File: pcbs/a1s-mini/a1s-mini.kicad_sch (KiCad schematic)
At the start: 47 parts, among them J1 UART1, J2 SJ-3524-SMT-TR-PI, J3 Audio Out, J4 UART0, Q3 BC818, Q4 MBT3904DW1, Q6 MBT3904DW1, U1 ESP32 A1S, U2 AZ1117CH-3.3TRG1

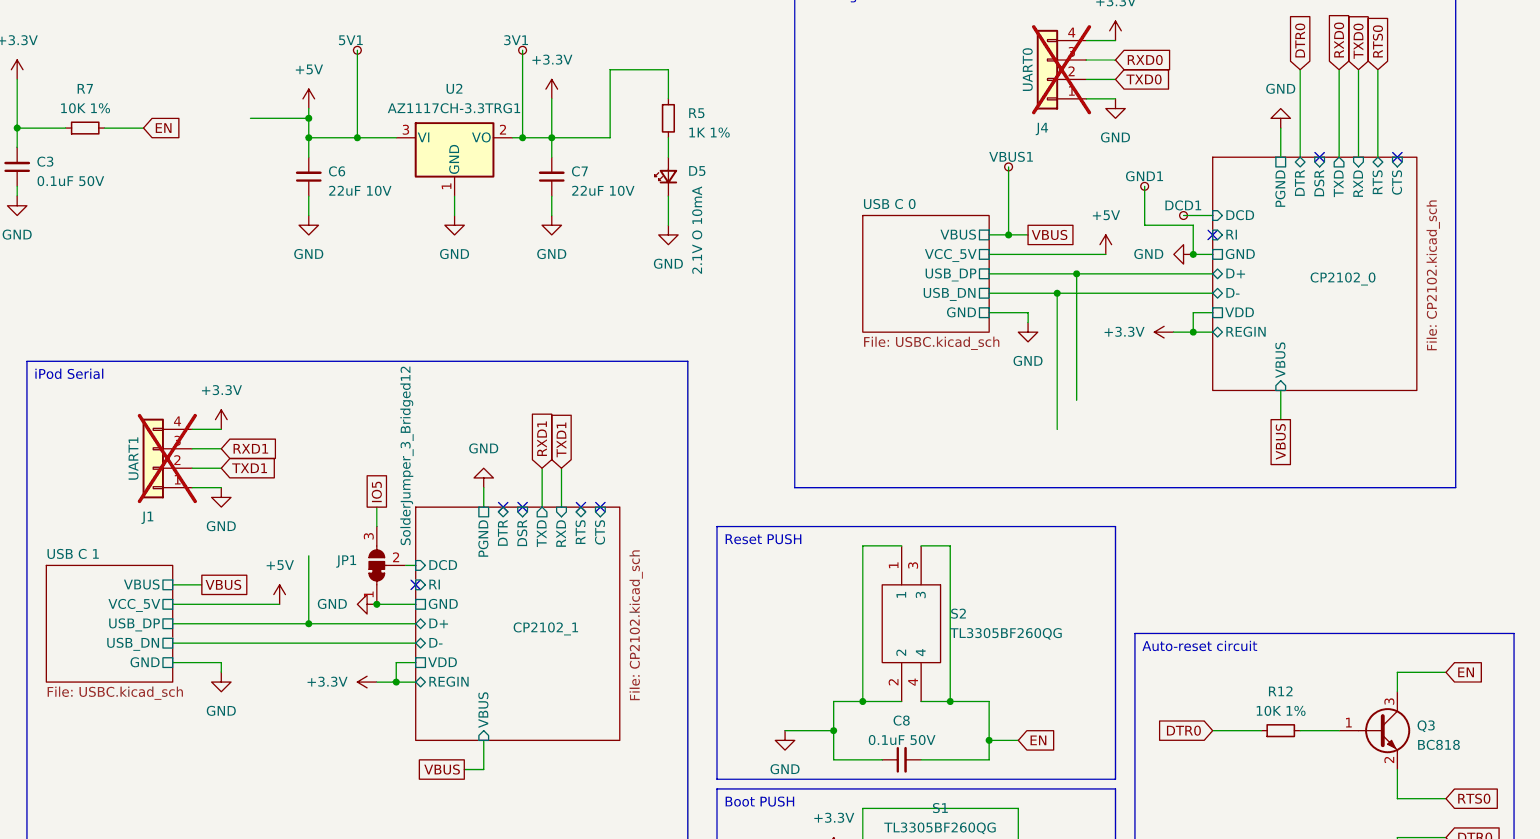
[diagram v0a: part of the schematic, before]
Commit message: Move to CP2102 non N
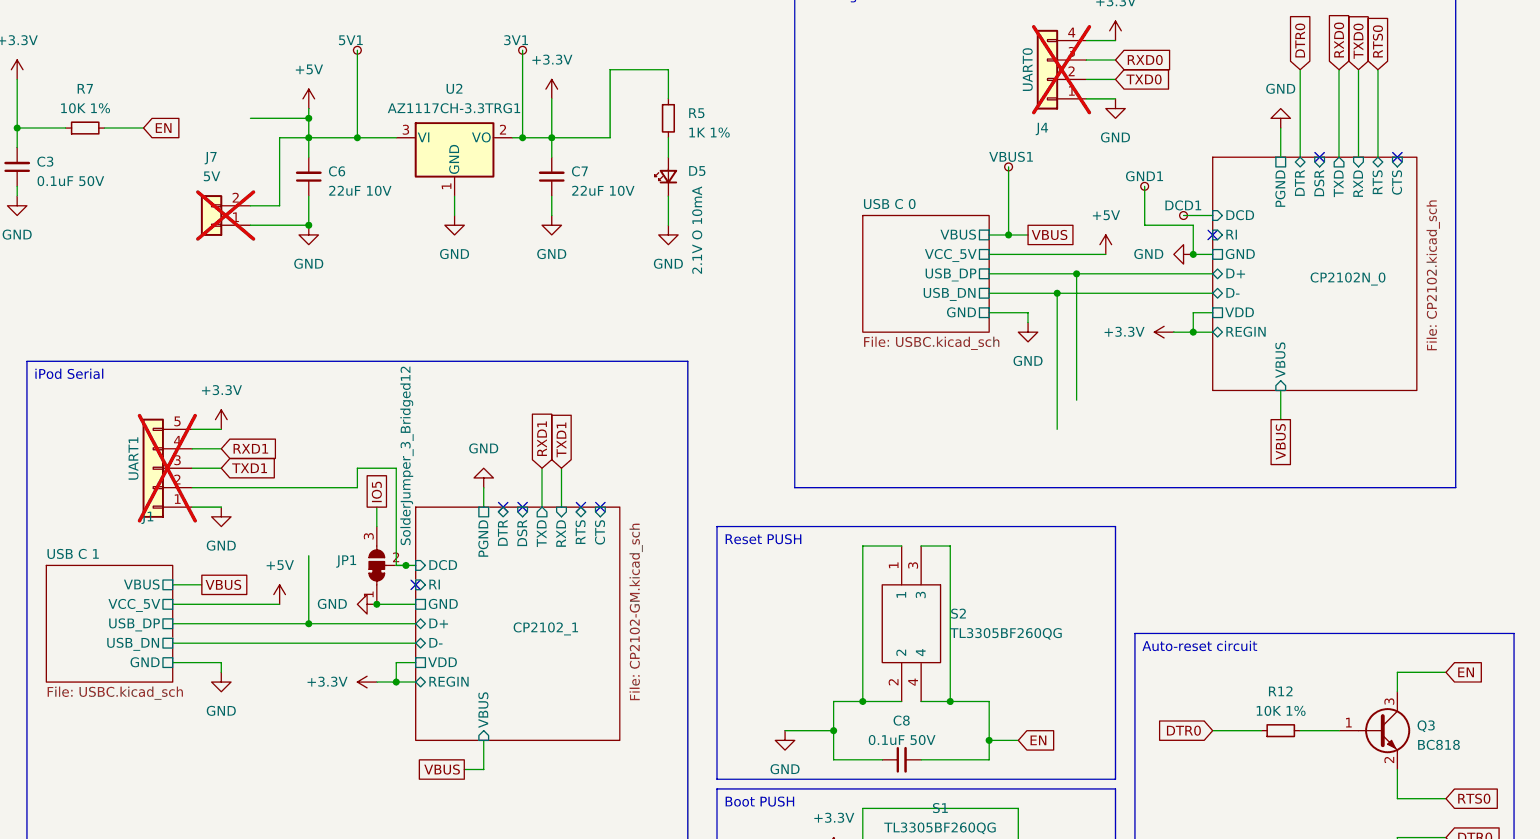
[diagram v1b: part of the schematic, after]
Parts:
- added J7: 5V, Connector_PinHeader_2.54mm:PinHeader_1x02_P2.54mm_Vertical, symbol Connector_Generic:Conn_01x02
- J1: symbol Connector_Generic:Conn_01x04 -> Connector_Generic:Conn_01x05
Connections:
- net +3.3V: now also J1.5 (Pin_5); no longer J1.4 (Pin_4)
- net +5V: now also J7.2 (Pin_2)
- net CP2102_1/DCD: now also J1.2 (Pin_2)
- net GND: now also J7.1 (Pin_1)
- net RXD1: now also J1.4 (Pin_4); no longer J1.3 (Pin_3)
- net TXD1: now also J1.3 (Pin_3); no longer J1.2 (Pin_2)
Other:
- sheet CP2102_0 renamed CP2102N_0
- sheet CP2102_1: file CP2102.kicad_sch -> CP2102-GM.kicad_sch
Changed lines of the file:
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@@
 	)
 	(junction
+		(at 138.43 90.17)
+		(diameter 0)
+		(color 0 0 0 0)
+	)
+	(junction
+		(at 125.73 45.72)
+		(diameter 0)
+		(color 0 0 0 0)
+	)
+	(junction
 		(at 241.3 59.69)
 		(diameter 0)
@@
 	(wire
 		(pts
-			(xy 125.73 41.91) (xy 125.73 44.45)
-		)
-		(stroke
-			(width 0)
-			(type default)
-		)
-	)
-	(wire
-		(pts
 			(xy 157.48 34.29) (xy 157.48 36.83)
 		)
@@
 	(wire
 		(pts
+			(xy 121.92 43.18) (xy 121.92 34.29)
+		)
+		(stroke
+			(width 0)
+			(type default)
+		)
+	)
+	(wire
+		(pts
 			(xy 200.66 152.4) (xy 200.66 153.67)
 		)
@@
 	(wire
 		(pts
+			(xy 125.73 41.91) (xy 125.73 45.72)
+		)
+		(stroke
+			(width 0)
+			(type default)
+		)
+	)
+	(wire
+		(pts
 			(xy 134.62 105.41) (xy 137.16 105.41)
 		)
@@
 	(wire
 		(pts
+			(xy 132.08 77.47) (xy 137.16 77.47)
+		)
+		(stroke
+			(width 0)
+			(type default)
+		)
+	)
+	(wire
+		(pts
 			(xy 78.74 147.32) (xy 78.74 149.86)
 		)
@@
 	(wire
 		(pts
+			(xy 118.11 45.72) (xy 125.73 45.72)
+		)
+		(stroke
+			(width 0)
+			(type default)
+		)
+	)
+	(wire
+		(pts
 			(xy 27.94 22.86) (xy 29.21 22.86)
 		)
@@
 	(wire
 		(pts
+			(xy 118.11 43.18) (xy 121.92 43.18)
+		)
+		(stroke
+			(width 0)
+			(type default)
+		)
+	)
+	(wire
+		(pts
 			(xy 67.31 38.1) (xy 71.12 38.1)
 		)
@@
 	(wire
 		(pts
+			(xy 137.16 77.47) (xy 137.16 90.17)
+		)
+		(stroke
+			(width 0)
+			(type default)
+		)
+	)
+	(wire
+		(pts
 			(xy 203.2 87.63) (xy 198.12 87.63)
 		)
@@
 	(wire
 		(pts
+			(xy 137.16 90.17) (xy 138.43 90.17)
+		)
+		(stroke
+			(width 0)
+			(type default)
+		)
+	)
+	(wire
+		(pts
 			(xy 262.89 25.4) (xy 262.89 36.83)
 		)
@@
 	(wire
 		(pts
+			(xy 110.49 80.01) (xy 132.08 80.01)
+		)
+		(stroke
+			(width 0)
+			(type default)
+		)
+	)
+	(wire
+		(pts
 			(xy 255.27 111.76) (xy 260.35 111.76)
 		)
@@
 	(wire
 		(pts
-			(xy 110.49 80.01) (xy 114.3 80.01)
+			(xy 149.86 173.99) (xy 151.13 173.99)
 		)
 		(stroke
@@
 	(wire
 		(pts
-			(xy 149.86 173.99) (xy 151.13 173.99)
+			(xy 219.71 57.15) (xy 219.71 58.42)
 		)
 		(stroke
@@
 	(wire
 		(pts
-			(xy 219.71 57.15) (xy 219.71 58.42)
+			(xy 29.21 25.4) (xy 17.78 25.4)
 		)
 		(stroke
@@
 	(wire
 		(pts
-			(xy 29.21 25.4) (xy 17.78 25.4)
+			(xy 267.97 158.75) (xy 267.97 161.29)
 		)
 		(stroke
@@
 	(wire
 		(pts
-			(xy 267.97 158.75) (xy 267.97 161.29)
+			(xy 234.95 45.72) (xy 234.95 40.64)
 		)
 		(stroke
@@
 	(wire
 		(pts
-			(xy 234.95 45.72) (xy 234.95 40.64)
+			(xy 125.73 88.9) (xy 125.73 97.79)
 		)
 		(stroke
@@
 	(wire
 		(pts
-			(xy 125.73 88.9) (xy 125.73 97.79)
+			(xy 121.92 34.29) (xy 125.73 34.29)
 		)
 		(stroke
@@
 	(wire
 		(pts
+			(xy 110.49 82.55) (xy 114.3 82.55)
+		)
+		(stroke
+			(width 0)
+			(type default)
+		)
+	)
+	(wire
+		(pts
 			(xy 267.97 104.14) (xy 267.97 106.68)
 		)
@@
 	(wire
 		(pts
+			(xy 132.08 80.01) (xy 132.08 77.47)
+		)
+		(stroke
+			(width 0)
+			(type default)
+		)
+	)
+	(wire
+		(pts
 			(xy 252.73 33.02) (xy 252.73 36.83)
 		)
@@
 	)
 	(symbol
+		(lib_id "Connector_Generic:Conn_01x02")
+		(at 113.03 45.72 180)
+		(unit 1)
+		(exclude_from_sim no)
+		(in_bom no)
+		(on_board yes)
+		(dnp yes)
+		(fields_autoplaced yes)
+		(property "Reference" "J7"
+			(at 113.03 36.83 0)
+			(effects
+				(font
+					(size 1.27 1.27)
+				)
+			)
+		)
+		(property "Value" "5V"
+			(at 113.03 39.37 0)
+			(effects
+				(font
+					(size 1.27 1.27)
+				)
+			)
+		)
+		(property "Footprint" "Connector_PinHeader_2.54mm:PinHeader_1x02_P2.54mm_Vertical"
+			(at 113.03 45.72 0)
+			(effects
+				(font
+					(size 1.27 1.27)
+				)
+				(hide yes)
+			)
+		)
+		(property "Datasheet" "~"
+			(at 113.03 45.72 0)
+			(effects
+				(font
+					(size 1.27 1.27)
+				)
+				(hide yes)
+			)
+		)
+		(property "Description" "Generic connector, single row, 01x02, script generated (kicad-library-utils/schlib/autogen/connector/)"
+			(at 113.03 45.72 0)
+			(effects
+				(font
+					(size 1.27 1.27)
+				)
+				(hide yes)
+			)
+		)
+		(pin "1"
+		)
+		(pin "2"
+		)
+		(instances
+			(project ""
+				(path "/473bba75-08f8-4c6c-a9b2-aa3e95e63a5e"
+					(reference "J7")
+					(unit 1)
+				)
+			)
+		)
+	)
+	(symbol
 		(lib_id "power:GND")
-		(at 114.3 80.01 0)
+		(at 114.3 82.55 0)
 		(unit 1)
 		(exclude_from_sim no)
@@
 		(fields_autoplaced yes)
 		(property "Reference" "#PWR027"
-			(at 114.3 86.36 0)
+			(at 114.3 88.9 0)
 			(effects
 				(font
@@
 		)
 		(property "Value" "GND"
-			(at 114.3 85.09 0)
+			(at 114.3 87.63 0)
 			(effects
 				(font
@@
 		)
 		(property "Footprint" ""
-			(at 114.3 80.01 0)
+			(at 114.3 82.55 0)
 			(effects
 				(font
@@
 		)
 		(property "Datasheet" ""
-			(at 114.3 80.01 0)
+			(at 114.3 82.55 0)
 			(effects
 				(font
@@
 		)
 		(property "Description" ""
-			(at 114.3 80.01 0)
+			(at 114.3 82.55 0)
 			(effects
 				(font
@@
 	(symbol
 		(lib_id "power:GND")
-		(at 125.73 44.45 0)
+		(at 125.73 45.72 0)
 		(unit 1)
 		(exclude_from_sim no)
@@
 		(fields_autoplaced yes)
 		(property "Reference" "#PWR031"
-			(at 125.73 50.8 0)
+			(at 125.73 52.07 0)
 			(effects
 				(font
@@
 		)
 		(property "Value" "GND"
-			(at 125.73 49.53 0)
+			(at 125.73 50.8 0)
 			(effects
 				(font
@@
 		)
 		(property "Footprint" ""
-			(at 125.73 44.45 0)
+			(at 125.73 45.72 0)
 			(effects
 				(font
@@
 		)
 		(property "Datasheet" ""
-			(at 125.73 44.45 0)
+			(at 125.73 45.72 0)
 			(effects
 				(font
@@
 		)
 		(property "Description" ""
-			(at 125.73 44.45 0)
+			(at 125.73 45.72 0)
 			(effects
 				(font
@@
 	)
 	(symbol
-		(lib_id "Connector_Generic:Conn_01x04")
+		(lib_id "Connector_Generic:Conn_01x05")
 		(at 105.41 77.47 180)
 		(unit 1)
@@
 			)
 		)
-		(property "Description" ""
+		(property "Description" "Generic connector, single row, 01x05, script generated (kicad-library-utils/schlib/autogen/connector/)"
 			(at 105.41 77.47 0)
 			(effects
@@
 					(size 1.27 1.27)
 				)
+				(hide yes)
 			)
 		)
@@
 		(pin "4"
 		)
+		(pin "5"
+		)
 		(instances
 			(project "a1s-mini"
@@
 			)
 		)
-		(property "Sheetfile" "CP2102.kicad_sch"
+		(property "Sheetfile" "CP2102-GM.kicad_sch"
 			(at 167.64 107.95 90)
 			(effects
@@
 			(color 0 0 0 0.0000)
 		)
-		(property "Sheetname" "CP2102_0"
+		(property "Sheetname" "CP2102N_0"
 			(at 256.54 53.34 0)
 			(effects

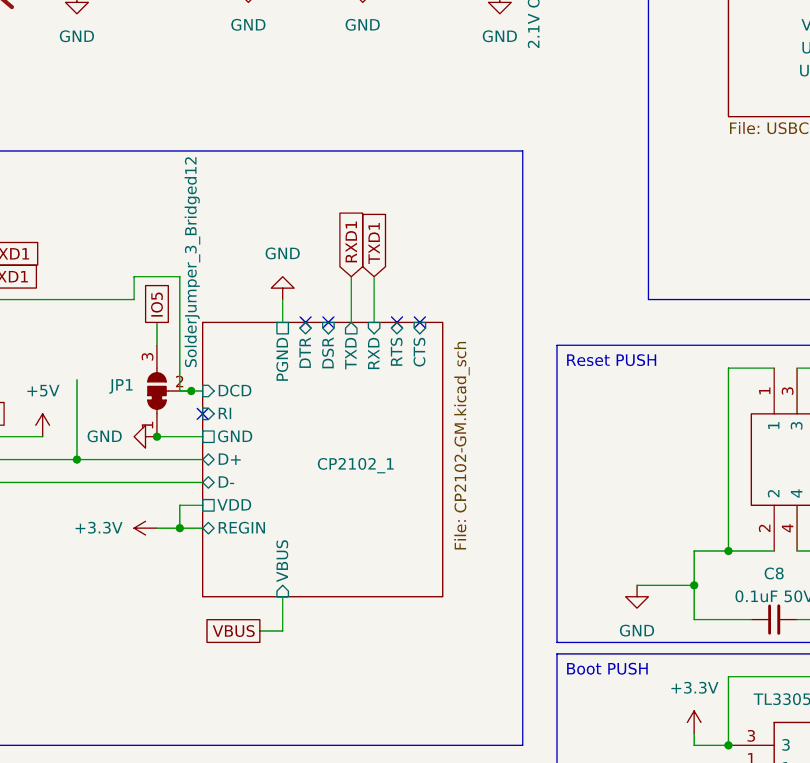
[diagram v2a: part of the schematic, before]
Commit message: A1S updated to CP2104
Version numbers also updated
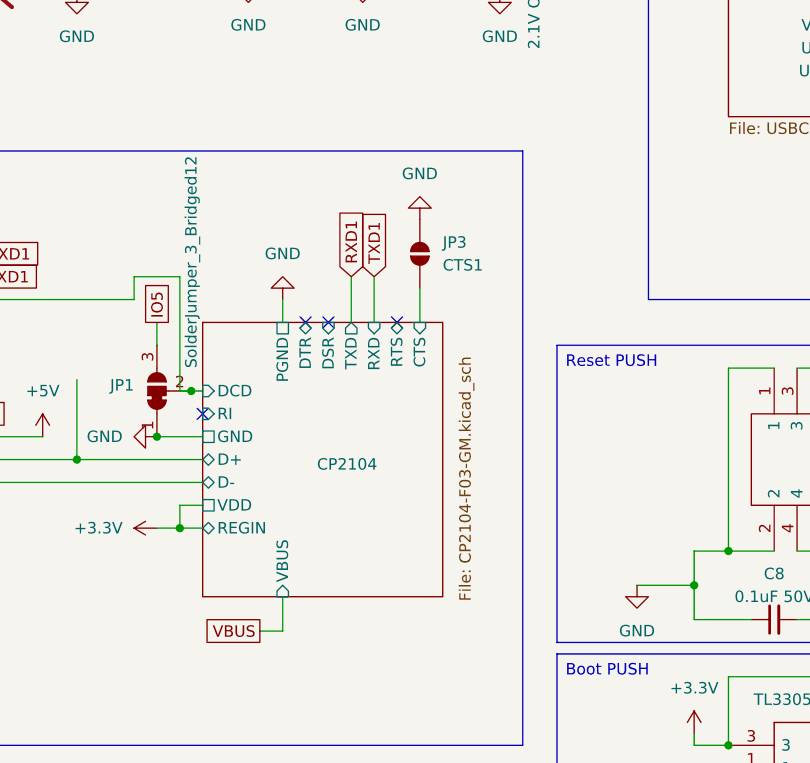
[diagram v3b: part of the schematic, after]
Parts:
- added JP3: CTS1, Jumper:SolderJumper-2_P1.3mm_Open_RoundedPad1.0x1.5mm, symbol Jumper:SolderJumper_2_Open
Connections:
- net CP2104/CTS: now also JP3.1 (A)
- net GND: now also JP3.2 (B)
- no-connect marks 30 -> 29
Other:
- sheet CP2102_1 renamed CP2104
- sheet CP2104: file CP2102-GM.kicad_sch -> CP2104-F03-GM.kicad_sch
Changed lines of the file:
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@@
 	(title_block
 		(title "A1S Mini Board")
-		(date "2025-10-05")
-		(rev "0.3.2")
+		(date "2025-10-22")
+		(rev "0.4.0")
 		(company "Martin Roger")
 	)
@@
 	)
 	(no_connect
-		(at 163.83 82.55)
-	)
-	(no_connect
 		(at 67.31 60.96)
 	)
@@
 	(wire
 		(pts
+			(xy 163.83 78.74) (xy 163.83 82.55)
+		)
+		(stroke
+			(width 0)
+			(type default)
+		)
+	)
+	(wire
+		(pts
 			(xy 110.49 151.13) (xy 110.49 152.4)
 		)
@@
 	(symbol
 		(lib_id "power:GND")
+		(at 163.83 71.12 180)
+		(unit 1)
+		(exclude_from_sim no)
+		(in_bom yes)
+		(on_board yes)
+		(dnp no)
+		(fields_autoplaced yes)
+		(property "Reference" "#PWR053"
+			(at 163.83 64.77 0)
+			(effects
+				(font
+					(size 1.27 1.27)
+				)
+				(hide yes)
+			)
+		)
+		(property "Value" "GND"
+			(at 163.83 66.04 0)
+			(effects
+				(font
+					(size 1.27 1.27)
+				)
+			)
+		)
+		(property "Footprint" ""
+			(at 163.83 71.12 0)
+			(effects
+				(font
+					(size 1.27 1.27)
+				)
+				(hide yes)
+			)
+		)
+		(property "Datasheet" ""
+			(at 163.83 71.12 0)
+			(effects
+				(font
+					(size 1.27 1.27)
+				)
+				(hide yes)
+			)
+		)
+		(property "Description" ""
+			(at 163.83 71.12 0)
+			(effects
+				(font
+					(size 1.27 1.27)
+				)
+			)
+		)
+		(pin "1"
+		)
+		(instances
+			(project "a1s-mini"
+				(path "/473bba75-08f8-4c6c-a9b2-aa3e95e63a5e"
+					(reference "#PWR053")
+					(unit 1)
+				)
+			)
+		)
+	)
+	(symbol
+		(lib_id "power:GND")
 		(at 252.73 33.02 180)
 		(unit 1)
@@
 	)
 	(symbol
+		(lib_id "Jumper:SolderJumper_2_Open")
+		(at 163.83 74.93 90)
+		(unit 1)
+		(exclude_from_sim yes)
+		(in_bom no)
+		(on_board yes)
+		(dnp no)
+		(fields_autoplaced yes)
+		(property "Reference" "JP3"
+			(at 166.37 73.6599 90)
+			(effects
+				(font
+					(size 1.27 1.27)
+				)
+				(justify right)
+			)
+		)
+		(property "Value" "CTS1"
+			(at 166.37 76.1999 90)
+			(effects
+				(font
+					(size 1.27 1.27)
+				)
+				(justify right)
+			)
+		)
+		(property "Footprint" "Jumper:SolderJumper-2_P1.3mm_Open_RoundedPad1.0x1.5mm"
+			(at 163.83 74.93 0)
+			(effects
+				(font
+					(size 1.27 1.27)
+				)
+				(hide yes)
+			)
+		)
+		(property "Datasheet" "~"
+			(at 163.83 74.93 0)
+			(effects
+				(font
+					(size 1.27 1.27)
+				)
+				(hide yes)
+			)
+		)
+		(property "Description" "Solder Jumper, 2-pole, open"
+			(at 163.83 74.93 0)
+			(effects
+				(font
+					(size 1.27 1.27)
+				)
+				(hide yes)
+			)
+		)
+		(pin "1"
+		)
+		(pin "2"
+		)
+		(instances
+			(project ""
+				(path "/473bba75-08f8-4c6c-a9b2-aa3e95e63a5e"
+					(reference "JP3")
+					(unit 1)
+				)
+			)
+		)
+	)
+	(symbol
 		(lib_id "Jumper:SolderJumper_2_Bridged")
 		(at 17.78 49.53 270)
@@
 			(color 0 0 0 0.0000)
 		)
-		(property "Sheetname" "CP2102_1"
+		(property "Sheetname" "CP2104"
 			(at 152.4 99.06 0)
 			(effects
@@
 			)
 		)
-		(property "Sheetfile" "CP2102-GM.kicad_sch"
-			(at 167.64 107.95 90)
+		(property "Sheetfile" "CP2104-F03-GM.kicad_sch"
+			(at 168.148 113.538 90)
 			(effects
 				(font
